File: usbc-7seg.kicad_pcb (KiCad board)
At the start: 2 copper layers, 32.8 x 15 mm, 24 parts, among them J1 USB_C_Receptacle_USB2.0_14P, Q1 AO3400A, Q2 AO3400A, SW1 TS-1088-AR02016, U1 GS2816CX, U2 GS2816CX, U3 CH32V203GxUx, U4 XC6206P332MR-G, Y1 12MHz

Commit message: Some routing, setup board stackup properly
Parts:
- added C7: 100n, Capacitor_SMD:C_0402_1005Metric, F.Cu at (129.4, 109.9)
- added FB1: GZ1608D601TF, Inductor_SMD:L_0603_1608Metric, F.Cu at (132.5, 109.9)
- TP1, TP2, TP3, TP4, TP5: moved to B.Cu
- moved R3 16.6 mm to (129.9, 106.1), turned to 90 degrees
- moved TP1 11.7 mm to (127.9, 106.3), turned to 180 degrees
- moved TP5 10.8 mm to (127.8, 100.9), turned to 180 degrees
- moved TP4 9.88 mm to (130.5, 101.0), turned to 180 degrees
- moved TP3 8.12 mm to (130.5, 103.6), turned to 180 degrees
- moved TP2 6.81 mm to (127.8, 103.7), turned to 180 degrees
- moved C2 1.33 mm to (141.3, 108.9), turned to -90 degrees
- moved C1 1.24 mm to (135.9, 108.9)
- moved U4 0.62 mm to (138.6, 108.5), turned to -90 degrees
- moved C4 0.40 mm to (146.6, 105.0)
- moved C6 0.20 mm to (148.9, 100.8)
- moved C3 0.14 mm to (140.0, 104.2)
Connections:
- C1 pad 1: /VUSB -> Net-(U4-VI)
- U4 pad 3: /VUSB -> Net-(U4-VI)
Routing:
- net +3.3V: track 0.00 -> 27.3 mm
- net /~{RST}: track 0.00 -> 24.1 mm, vias 0 -> 2
- net /VUSB: track 0.00 -> 14.5 mm
- net Net-(Q1-D): track 0.00 -> 13.2 mm
- net /SWCLK: track 0.00 -> 12.0 mm
- net /SWDIO: track 0.00 -> 11.5 mm
- net /LED_DP2: track 0.00 -> 10.9 mm
- net Net-(Q2-D): track 0.00 -> 10.8 mm
- net Net-(U3-OSC_IN/PD0): track 0.00 -> 7.09 mm
- net Net-(U3-OSC_OUT/PD1): track 0.00 -> 5.59 mm
- net /LED_G: track 0.00 -> 4.98 mm
- net /MSB_EN: track 0.00 -> 4.90 mm
- net /LED_DP1: track 0.00 -> 4.30 mm
- net GND: track 0.00 -> 3.92 mm
- net /LED_F: track 0.00 -> 3.65 mm
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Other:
- copper layers 2 -> 4

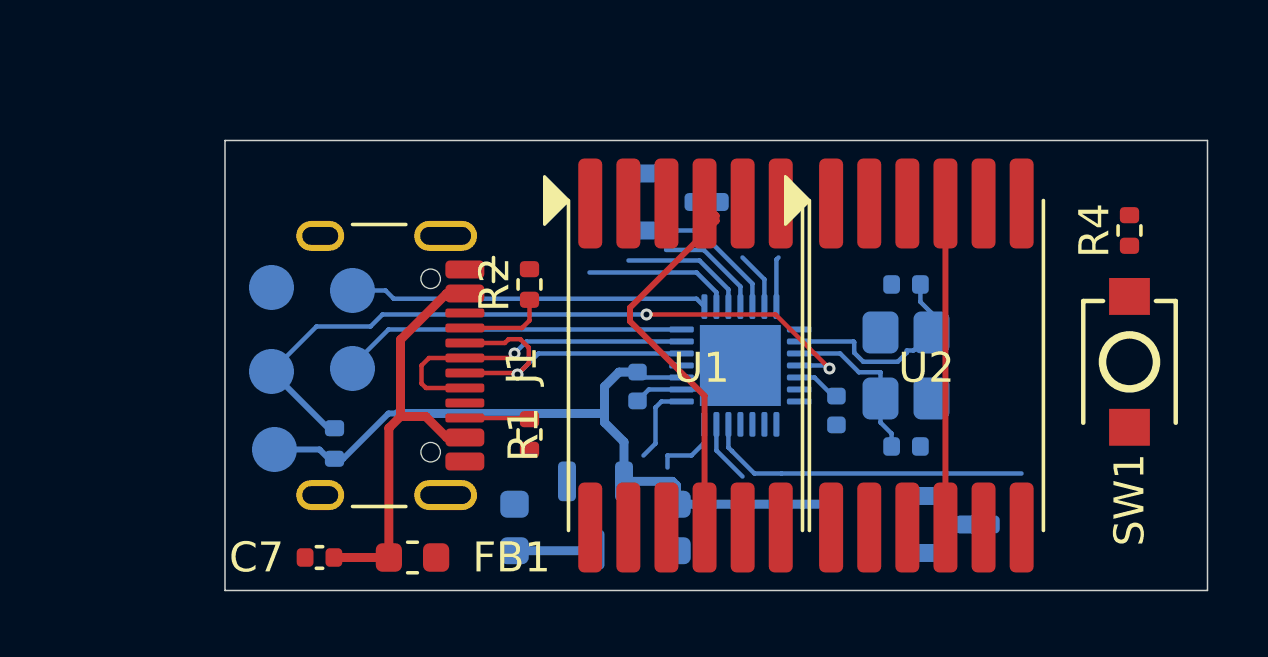
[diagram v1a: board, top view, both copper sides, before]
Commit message: Routing complete, DRC todo
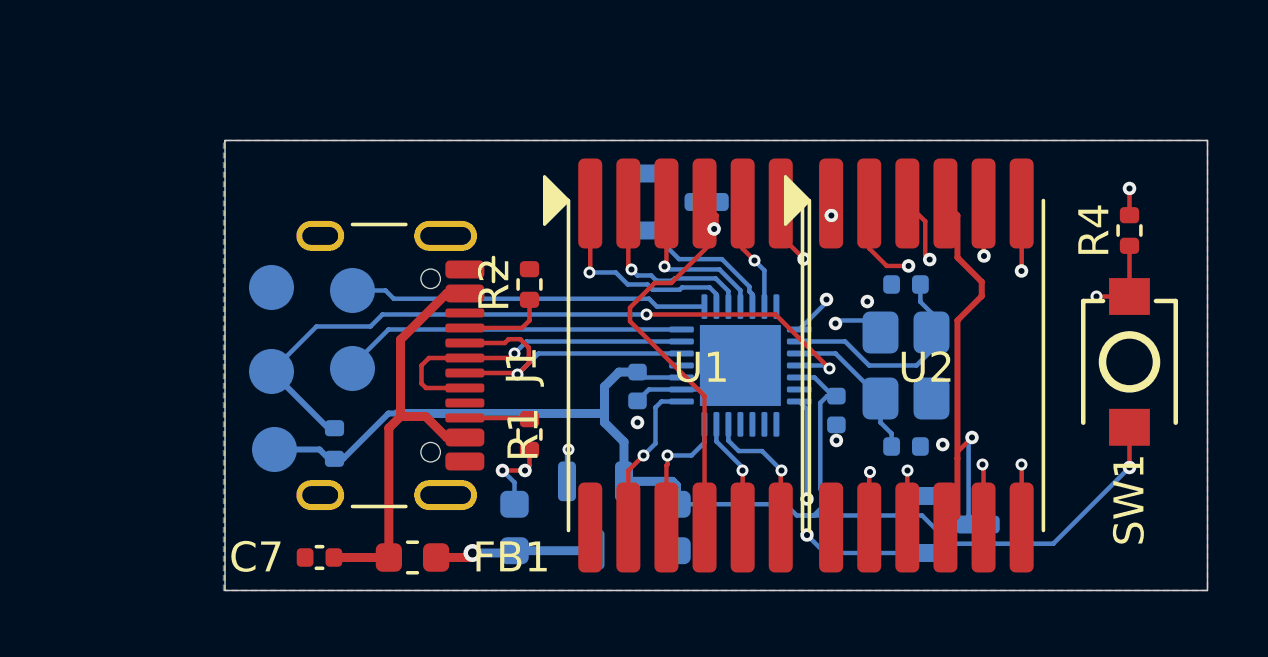
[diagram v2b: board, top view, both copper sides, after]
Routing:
- net +3.3V: track 27.3 -> 44.3 mm, vias 0 -> 1
- net /LED_DP1: track 4.30 -> 19.3 mm, vias 0 -> 2
- net Net-(U3-BOOT0/PB8): track 0.00 -> 14.0 mm, vias 0 -> 2
- net /LED_F: track 3.65 -> 17.1 mm, vias 0 -> 2
- net /LED_C: track 2.10 -> 15.5 mm, vias 0 -> 2
- net /LED_E: track 2.72 -> 15.5 mm, vias 0 -> 2
- net /LED_D: track 2.42 -> 15.1 mm, vias 0 -> 2
- net /LED_A: track 1.94 -> 14.2 mm, vias 0 -> 2
- net /LED_B: track 0.00 -> 11.3 mm, vias 0 -> 2
- net /LED_G: track 4.98 -> 16.2 mm, vias 0 -> 2
- net /LSB_EN: track 0.00 -> 8.62 mm, vias 0 -> 2
- net /LED_DP2: track 10.9 -> 16.3 mm, vias 0 -> 2
- net Net-(Q2-D): track 10.8 -> 15.8 mm, vias 0 -> 1
- net GND: track 3.92 -> 8.69 mm, vias 0 -> 9
- net Net-(U4-VI): track 2.72 -> 5.26 mm, vias 0 -> 1
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- added copper zone on B.Cu, net GND
- added copper zone on F.Cu, net GND
- added copper zone on In2.Cu, net GND

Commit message: Passing DRC
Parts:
- moved TP2 0.49 mm to (128.2, 103.5)
- moved TP5 0.46 mm to (128.2, 101.0)
- moved TP1 0.46 mm to (128.2, 106.0)
- moved R3 0.35 mm to (130.2, 106.1)
- moved TP3 0.27 mm to (130.8, 103.5)
- moved TP4 0.25 mm to (130.8, 101.0)
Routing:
- net /~{RST}: track 23.9 -> 24.5 mm
- net +3.3V: track 44.3 -> 44.9 mm
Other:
- board text added: "250824 V1"

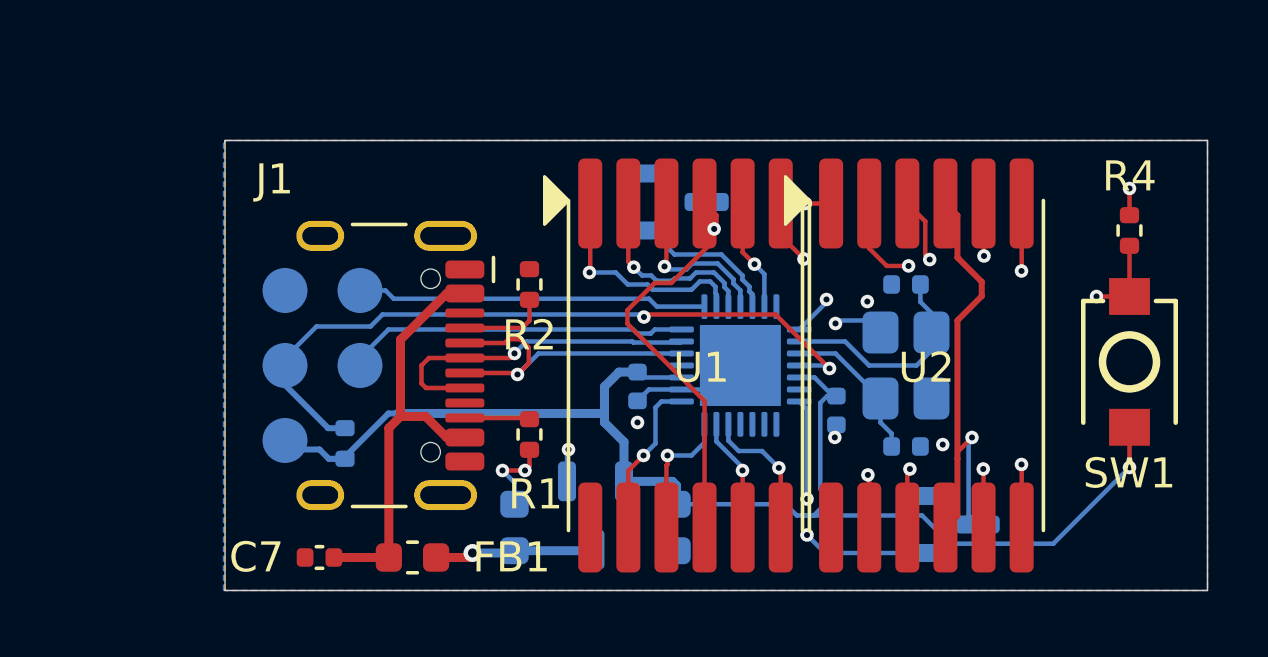
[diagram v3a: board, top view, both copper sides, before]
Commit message: Fix USB-C CC resistors
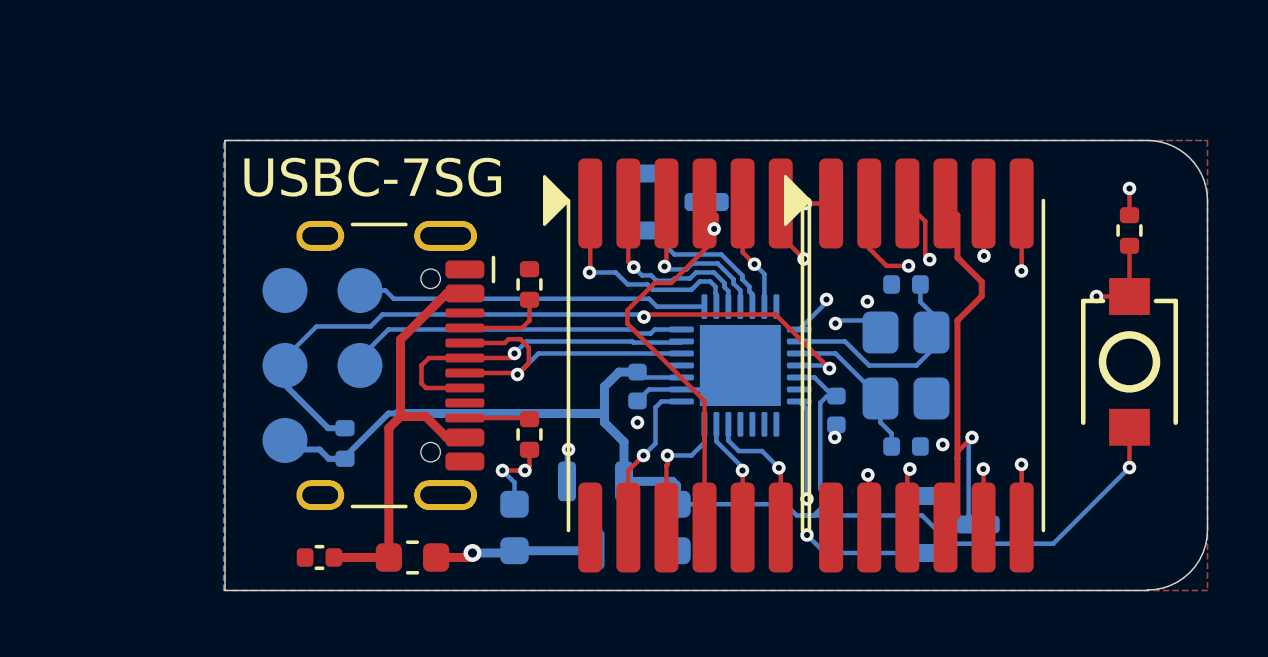
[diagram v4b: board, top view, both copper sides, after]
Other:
- outline, holes or cut-outs redrawn
- board text added: "${REFERENCE}"
- board text added: "C"
- board text added: "D"
- board text added: "R"
- board text added: "USBC-7SG"

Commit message: First gerber export
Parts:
- R1, R2: value 56K -> 5.1K
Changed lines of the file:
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@@
 			(plot_on_all_layers_selection 0x00000000_00000000_00000000_00000000)
 			(disableapertmacros no)
-			(usegerberextensions no)
+			(usegerberextensions yes)
 			(usegerberattributes yes)
 			(usegerberadvancedattributes yes)
@@
 			(sketchdnponfab yes)
 			(crossoutdnponfab yes)
-			(subtractmaskfromsilk no)
+			(subtractmaskfromsilk yes)
 			(outputformat 1)
 			(mirror no)
-			(drillshape 1)
+			(drillshape 0)
 			(scaleselection 1)
-			(outputdirectory "")
+			(outputdirectory "Gerber/")
 		)
 	)
@@
 			)
 		)
-		(property "Value" "56K"
+		(property "Value" "5.1K"
 			(at 0 1.17 90)
 			(layer "F.Fab")
@@
 			)
 		)
-		(property "Value" "56K"
+		(property "Value" "5.1K"
 			(at 0 1.17 90)
 			(layer "F.Fab")

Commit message: Add JLCPCB part numbers for all parts
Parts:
- U1, U2: value GS2816CX -> GS2816CW-G
- U3: value CH32V203GxUx -> CH32V203G6U6
